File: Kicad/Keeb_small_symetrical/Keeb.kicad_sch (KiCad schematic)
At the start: 19 parts, among them J1 MJ-4PP-9, SW10 CherryMX, SW11 CherryMX, SW13 CherryMX, SW14 CherryMX, SW15 CherryMX, SW16 CherryMX, SW17 CherryMX, SW18 CherryMX, SW19 CherryMX, SW20 CherryMX, SW3 CherryMX, SW4 CherryMX, SW5 CherryMX, SW6 CherryMX, SW7 CherryMX, SW8 CherryMX, SW9 CherryMX, U1 Pico

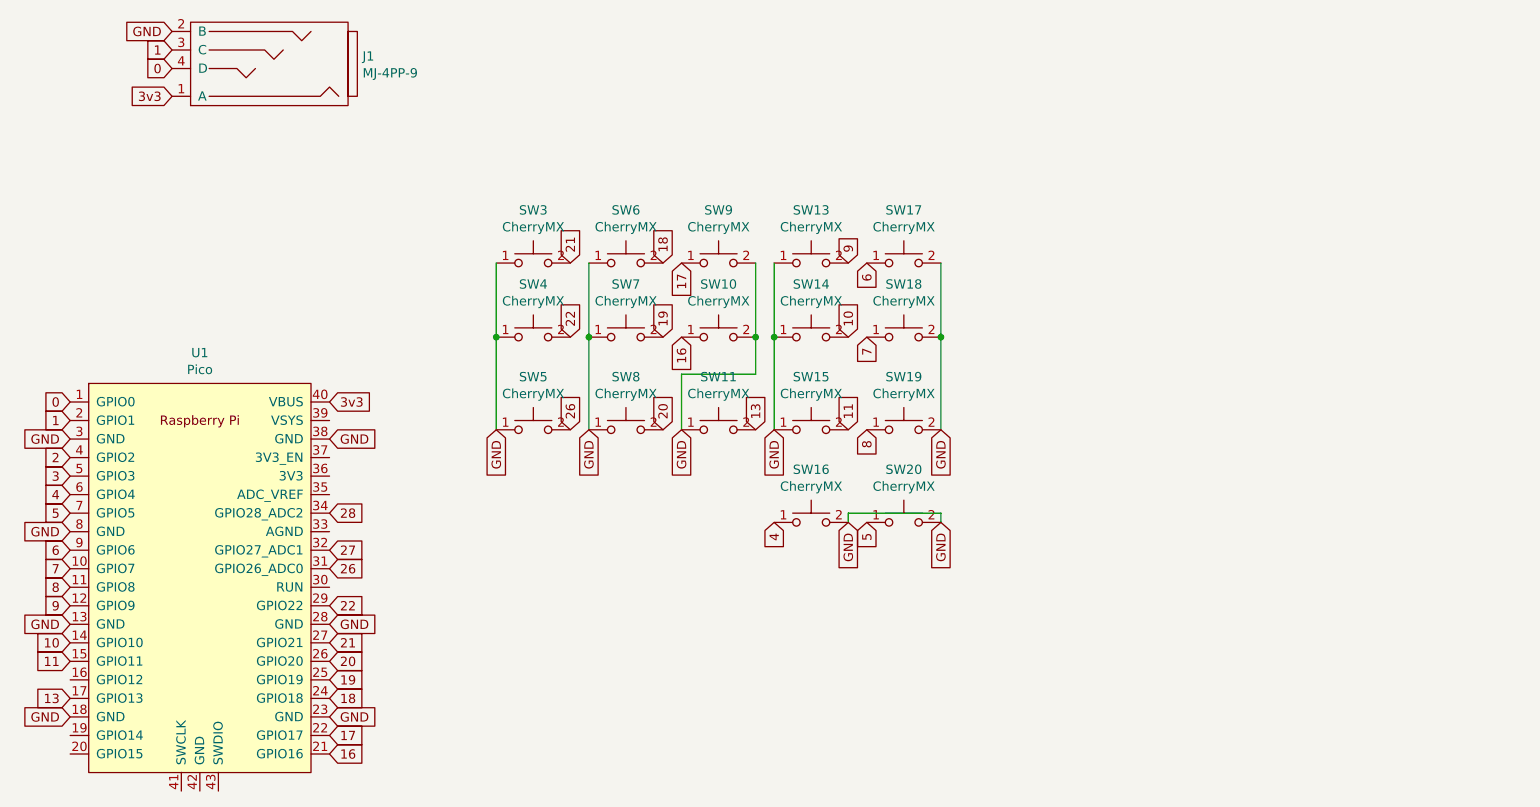
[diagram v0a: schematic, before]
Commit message: Added universal left-right pcb design, started work on hotswap variant
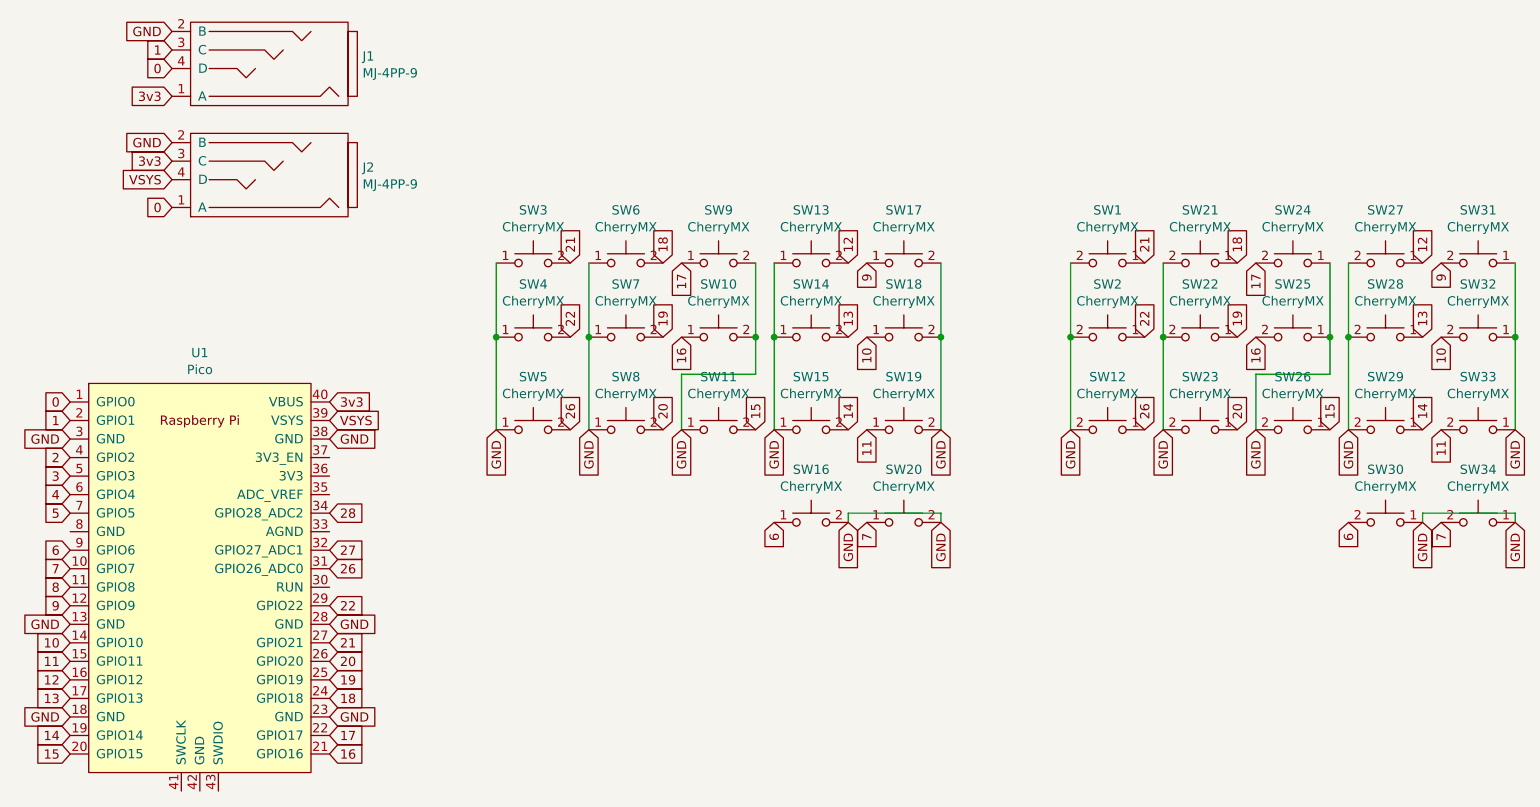
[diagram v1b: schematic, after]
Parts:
- added J2: MJ-4PP-9, MJ-4PP-9:MJ-4PP-9, symbol Keeb-rescue:MJ-4PP-9-MJ-4PP-9
- added SW1, SW12, SW2, SW21, SW22, SW23, SW24, SW25, SW26, SW27, SW28, SW29, SW30, SW31, SW32, SW33, SW34: CherryMX, ScottoKeebs_MX:MX_PCB_1.00u, symbol Keeb-rescue:CherryMX-CherryMX
- J1: footprint MJ-4PP-9:MJ-4PP-9_no_silk -> MJ-4PP-9:MJ-4PP-9
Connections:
- net 0: now also J2.1 (A)
- net 10: now also SW18.1, SW32.2; no longer SW14.2
- net 11: now also SW19.1, SW33.2; no longer SW15.2
- net 13: now also SW14.2, SW28.1; no longer SW11.2
- net 16: now also SW25.2
- net 17: now also SW24.2
- net 18: now also SW21.1
- net 19: now also SW22.1
- net 20: now also SW23.1
- net 21: now also SW1.1
- net 22: now also SW2.1
- net 26: now also SW12.1
- net 3v3: now also J2.3 (C)
- net 4: no longer SW16.1
- net 5: no longer SW20.1
- net 6: now also SW16.1, SW30.2; no longer SW17.1
- net 7: now also SW20.1, SW34.2; no longer SW18.1
- net 8: no longer SW19.1
- net 9: now also SW17.1, SW31.2; no longer SW13.2
- net GND: now also J2.2 (B), SW1.2, SW12.2, SW2.2, SW21.2, SW22.2, SW23.2, SW24.1, SW25.1, SW26.2, SW27.2, SW28.2, SW29.2, SW30.1, SW31.1, SW32.1, SW33.1, SW34.1; no longer U1.8 (GND)
- net 12: now reaches U1.16 (GPIO12)
- net 12: now also SW13.2, SW27.1
- net 14: now reaches U1.19 (GPIO14)
- net 14: now also SW15.2, SW29.1
- net 15: now reaches U1.20 (GPIO15)
- net 15: now also SW11.2, SW26.1
- net VSYS: now reaches U1.39 (VSYS)
- net VSYS: now also J2.4 (D)
